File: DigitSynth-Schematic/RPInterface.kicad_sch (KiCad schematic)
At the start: 1 part

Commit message: removed power schematic sheet as RPI5 has decoupling capacitors; fixed component value errors; buttons removed from RPI5 sheet and added to ADC analog inputs; LED_VPLUS power line removed and replaced by +5V_PERIPH
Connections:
- net BTN_1: no longer names the net of J_RPI1.11 (Pin_11)
- net BTN_2: no longer names the net of J_RPI1.13 (Pin_13)
- net BTN_3: no longer names the net of J_RPI1.15 (Pin_15)
- net BTN_4: no longer names the net of J_RPI1.29 (Pin_29)
- no-connect marks 17 -> 21

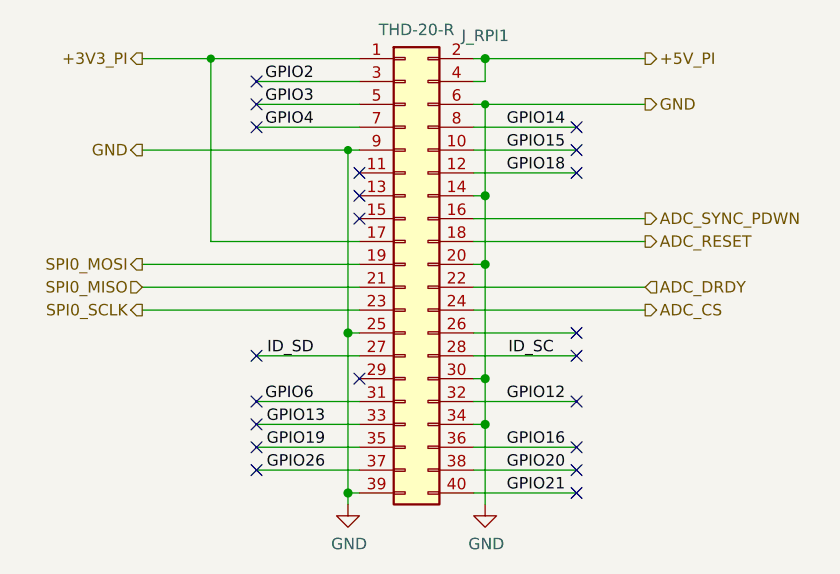
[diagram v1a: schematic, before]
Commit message: updated schematic for PCB design
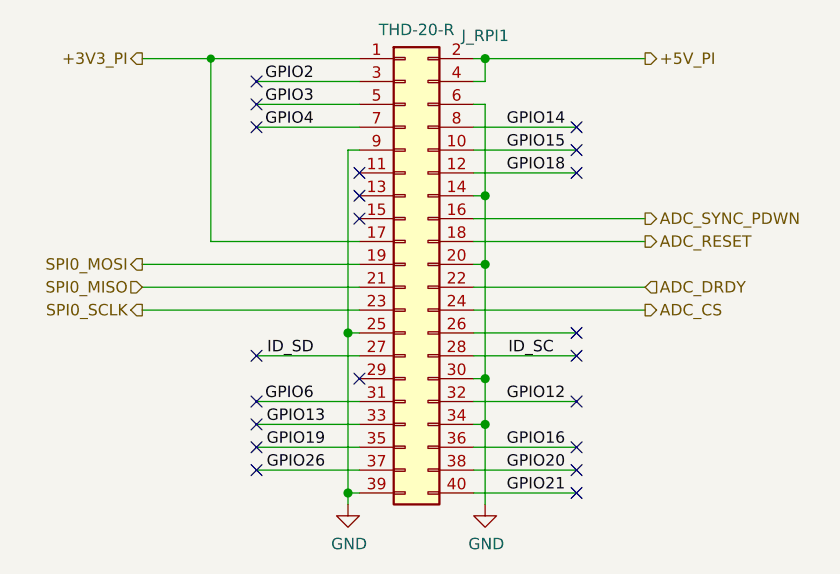
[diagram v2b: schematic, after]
